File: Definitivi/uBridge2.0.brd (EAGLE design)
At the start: 39.9 x 39.9 mm, 43 parts, among them IC4 AP6503SP-13

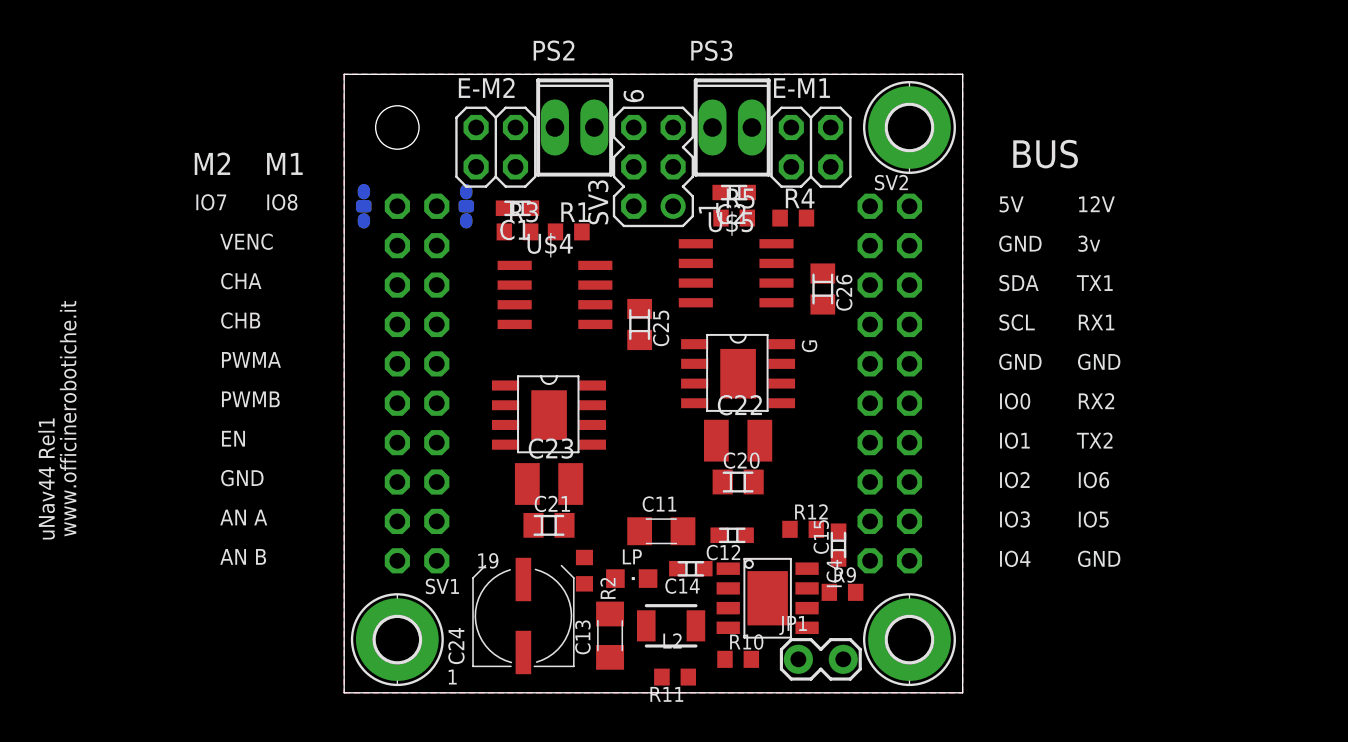
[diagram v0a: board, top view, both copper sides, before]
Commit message: add SATA connector
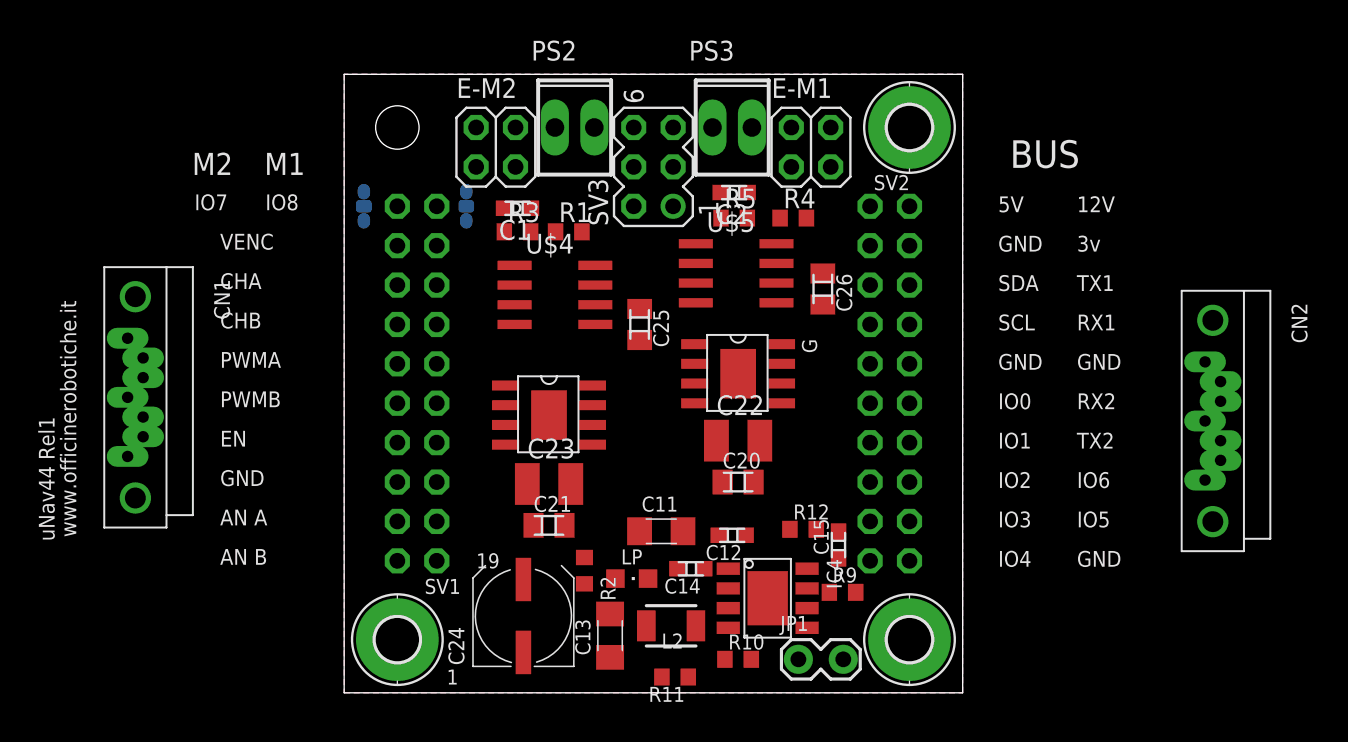
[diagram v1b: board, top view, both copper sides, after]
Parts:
- added CN1, CN2: SATA-7, OfficineRobotiche:SATA-5607-5102-SH
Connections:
- new net AUX1: CN2.2
- new net AUX2: CN1.2
- net EN1: now also CN2.3
- net EN2: now also CN1.3
- net GND: now also CN1.1, CN1.4, CN1.7, CN1.H1, CN1.H2, CN2.1, CN2.4, CN2.7, CN2.H1, CN2.H2
- net PWMA1: now also CN2.6
- net PWMA2: now also CN1.6
- net PWMB1: now also CN2.5
- net PWMB2: now also CN1.5
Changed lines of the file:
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@@
 <attribute name="OC_FARNELL" value="unknown" x="16.51" y="30.48" size="1.778" layer="27" rot="R90" display="off"/>
 </element>
+<element name="CN1" library="OfficineRobotiche" package="SATA-5607-5102-SH" value="SATA-7" x="-16.891" y="15.621" rot="R270"/>
+<element name="CN2" library="OfficineRobotiche" package="SATA-5607-5102-SH" value="SATA-7" x="52.578" y="14.097" rot="R270"/>
 </elements>
 <signals>
@@
 <contactref element="SV1" pad="9"/>
 <contactref element="U$2" pad="2TON"/>
-<wire x1="6.979" y1="15.113" x2="2.54" y2="17.78" width="0" layer="19" extent="1-1"/>
+<contactref element="CN2" pad="6"/>
+<wire x1="6.979" y1="15.113" x2="53.078" y2="16.637" width="0" layer="19" extent="1-1"/>
+<wire x1="2.54" y1="17.78" x2="6.979" y2="15.113" width="0" layer="19" extent="1-1"/>
 </signal>
 <signal name="PWMB1">
 <contactref element="SV1" pad="11"/>
 <contactref element="U$2" pad="3EN"/>
+<contactref element="CN2" pad="5"/>
+<wire x1="2.54" y1="15.24" x2="53.078" y2="15.367" width="0" layer="19" extent="1-1"/>
 <wire x1="6.979" y1="13.843" x2="2.54" y2="15.24" width="0" layer="19" extent="1-1"/>
 </signal>
@@
 <contactref element="SV1" pad="13"/>
 <contactref element="U$2" pad="4CS"/>
+<contactref element="CN2" pad="3"/>
+<wire x1="2.54" y1="12.7" x2="53.078" y2="12.827" width="0" layer="19" extent="1-1"/>
 <wire x1="6.979" y1="12.573" x2="2.54" y2="12.7" width="0" layer="19" extent="1-1"/>
 </signal>
@@
 <contactref element="SV1" pad="10"/>
 <contactref element="U$3" pad="2TON"/>
+<contactref element="CN1" pad="6"/>
 <wire x1="0" y1="17.78" x2="19.171" y2="17.78" width="0" layer="19" extent="1-1"/>
+<wire x1="-16.391" y1="18.161" x2="0" y2="17.78" width="0" layer="19" extent="1-1"/>
 </signal>
 <signal name="PWMB2">
 <contactref element="SV1" pad="12"/>
 <contactref element="U$3" pad="3EN"/>
+<contactref element="CN1" pad="5"/>
 <wire x1="0" y1="15.24" x2="19.171" y2="16.51" width="0" layer="19" extent="1-1"/>
+<wire x1="-16.391" y1="16.891" x2="0" y2="15.24" width="0" layer="19" extent="1-1"/>
 </signal>
 <signal name="EN2">
 <contactref element="SV1" pad="14"/>
 <contactref element="U$3" pad="4CS"/>
+<contactref element="CN1" pad="3"/>
 <wire x1="0" y1="12.7" x2="19.171" y2="15.24" width="0" layer="19" extent="1-1"/>
+<wire x1="-16.391" y1="14.351" x2="0" y2="12.7" width="0" layer="19" extent="1-1"/>
 </signal>
 <signal name="IO4">
@@
 <contactref element="SV3" pad="2"/>
 <contactref element="SV3" pad="1"/>
+<contactref element="CN2" pad="1"/>
+<contactref element="CN2" pad="7"/>
+<contactref element="CN2" pad="4"/>
+<contactref element="CN1" pad="1"/>
+<contactref element="CN1" pad="7"/>
+<contactref element="CN1" pad="4"/>
+<contactref element="CN2" pad="H2"/>
+<contactref element="CN2" pad="H1"/>
+<contactref element="CN1" pad="H2"/>
+<contactref element="CN1" pad="H1"/>
 <wire x1="30.48" y1="25.4" x2="33.02" y2="33.02" width="0" layer="19" extent="1-1"/>
 <wire x1="27.432" y1="21.606" x2="30.48" y2="25.4" width="0" layer="19" extent="1-1"/>
@@
 <wire x1="15.24" y1="27.94" x2="17.78" y2="27.94" width="0" layer="19" extent="1-1"/>
 <wire x1="25.4" y1="30.48" x2="20.867" y2="28.829" width="0" layer="19" extent="1-1"/>
-<wire x1="6.897" y1="27.813" x2="15.24" y2="27.94" width="0" layer="19" extent="1-1"/>
-<wire x1="6.897" y1="26.289" x2="6.897" y2="27.813" width="0" layer="19" extent="1-1"/>
-<wire x1="5.08" y1="30.48" x2="6.897" y2="27.813" width="0" layer="19" extent="1-1"/>
-<wire x1="4.445" y1="28.878" x2="5.08" y2="30.48" width="0" layer="19" extent="16-16"/>
-<wire x1="-2.159" y1="28.878" x2="4.445" y2="28.878" width="0" layer="19" extent="16-16"/>
 <wire x1="33.02" y1="0" x2="25.8572" y2="-1.27" width="0" layer="19" extent="1-1"/>
 <wire x1="33.02" y1="5.08" x2="33.02" y2="0" width="0" layer="19" extent="1-1"/>
 <wire x1="0" y1="0" x2="8.128" y2="-0.826" width="0" layer="19" extent="1-1"/>
+<wire x1="6.897" y1="27.813" x2="15.24" y2="27.94" width="0" layer="19" extent="1-1"/>
+<wire x1="6.897" y1="26.289" x2="6.897" y2="27.813" width="0" layer="19" extent="1-1"/>
+<wire x1="4.445" y1="28.878" x2="6.897" y2="27.813" width="0" layer="19" extent="1-16"/>
+<wire x1="5.08" y1="30.48" x2="4.445" y2="28.878" width="0" layer="19" extent="16-16"/>
+<wire x1="-2.159" y1="28.878" x2="4.445" y2="28.878" width="0" layer="19" extent="16-16"/>
+<wire x1="-16.891" y1="9.1313" x2="0" y2="0" width="0" layer="19" extent="1-1"/>
+<wire x1="-17.391" y1="11.811" x2="-16.891" y2="9.1313" width="0" layer="19" extent="1-1"/>
+<wire x1="-17.391" y1="15.621" x2="-17.391" y2="11.811" width="0" layer="19" extent="1-1"/>
+<wire x1="-17.391" y1="19.431" x2="-17.391" y2="15.621" width="0" layer="19" extent="1-1"/>
+<wire x1="-16.891" y1="22.1107" x2="-17.391" y2="19.431" width="0" layer="19" extent="1-1"/>
+<wire x1="52.578" y1="20.5867" x2="-17.391" y2="19.431" width="0" layer="19" extent="1-1"/>
+<wire x1="52.078" y1="17.907" x2="52.578" y2="20.5867" width="0" layer="19" extent="1-1"/>
+<wire x1="52.078" y1="14.097" x2="52.078" y2="17.907" width="0" layer="19" extent="1-1"/>
+<wire x1="52.078" y1="10.287" x2="52.078" y2="14.097" width="0" layer="19" extent="1-1"/>
+<wire x1="52.578" y1="7.6073" x2="52.078" y2="10.287" width="0" layer="19" extent="1-1"/>
 </signal>
 <signal name="TX2">
@@
 <wire x1="24.444" y1="24.257" x2="26.377" y2="27.178" width="0" layer="19" extent="1-1"/>
 </signal>
+<signal name="AUX1">
+<contactref element="CN2" pad="2"/>
+</signal>
+<signal name="AUX2">
+<contactref element="CN1" pad="2"/>
+</signal>
 </signals>
